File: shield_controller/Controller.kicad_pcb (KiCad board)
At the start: 2 copper layers, 68.6 x 53.3 mm, 16 parts, among them J1 Input Power, J2 Track, J3 DCC, J4 Calc, U1 LM7805_TO220, U2 LMD18200T

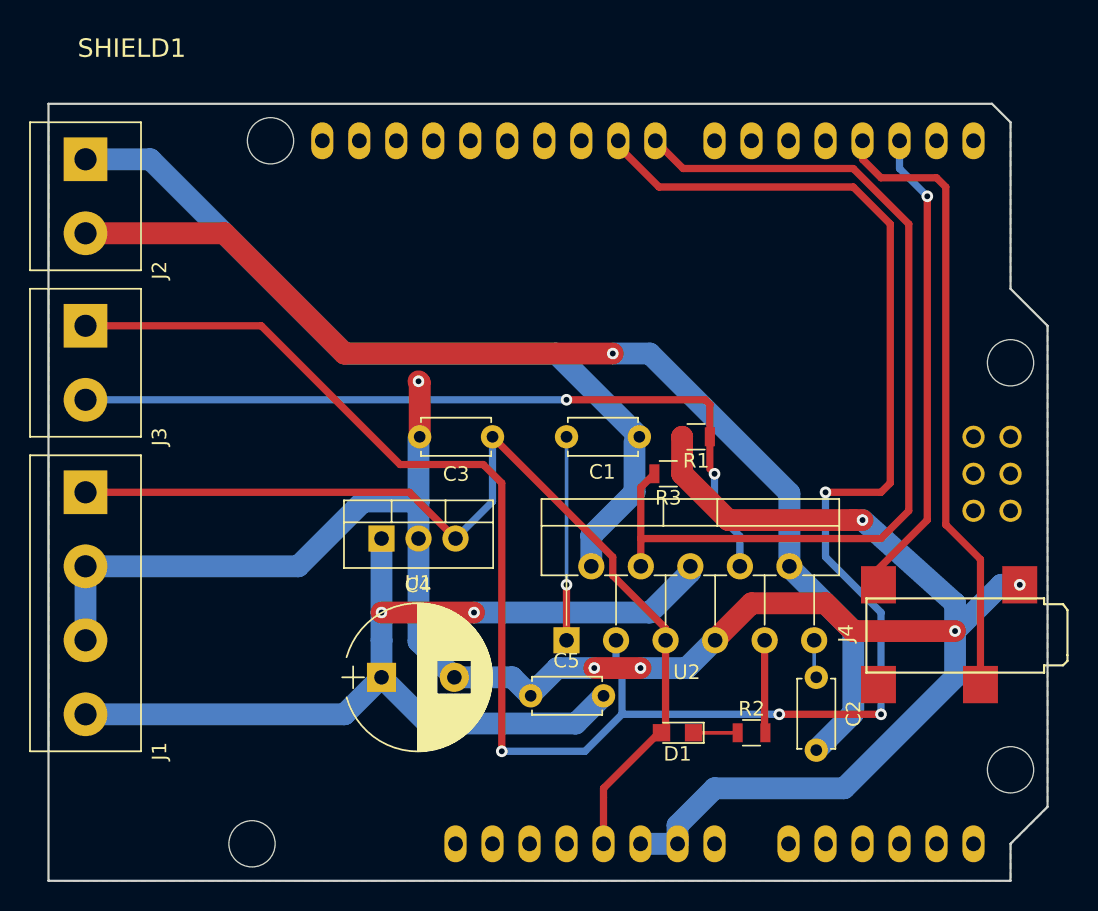
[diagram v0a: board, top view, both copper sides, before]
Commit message: Updating Christopher's shield controller to current fabbed version
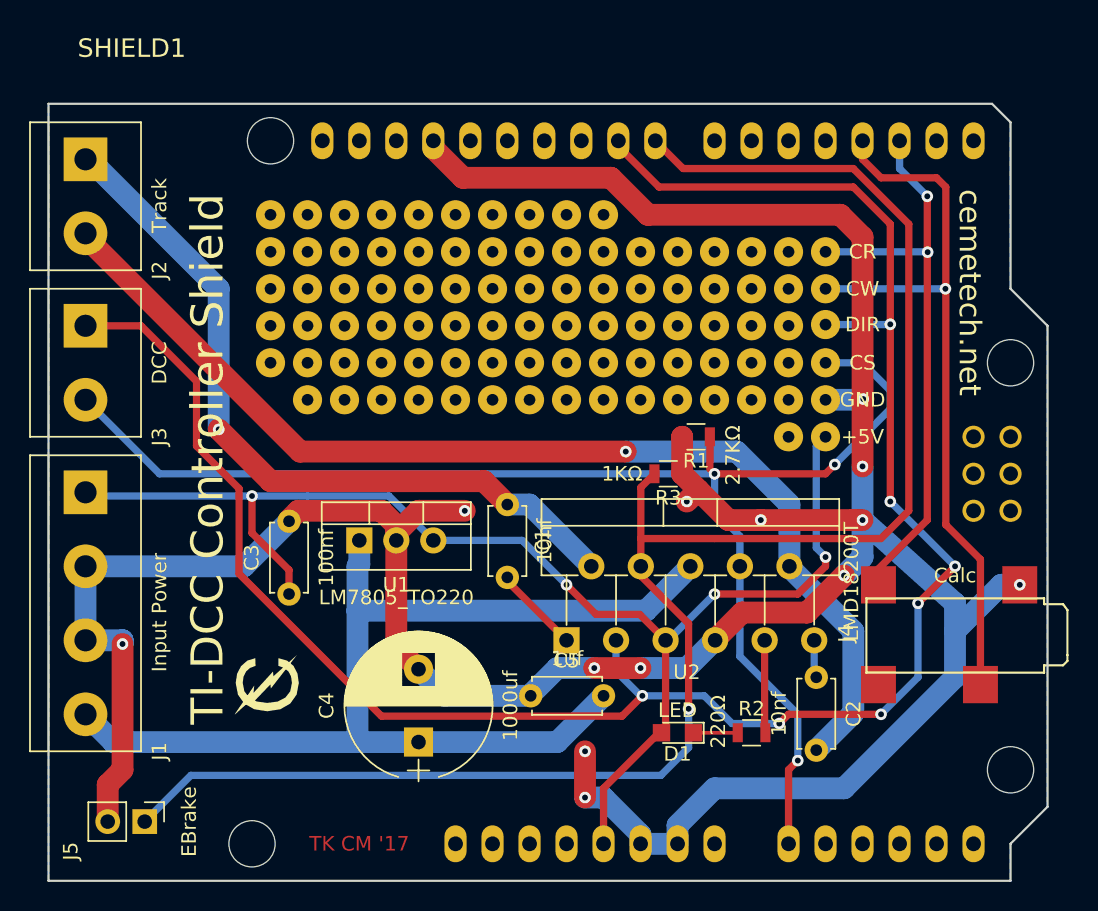
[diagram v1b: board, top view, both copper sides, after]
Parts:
- added ?: , Wire_Pads:SolderWirePad_single_0-8mmDrill, F.Cu at (149.9, 73.7)
- added ?: , Wire_Pads:SolderWirePad_single_0-8mmDrill, F.Cu at (162.6, 63.5)
- added ?: , Wire_Pads:SolderWirePad_single_0-8mmDrill, F.Cu at (165.1, 63.5)
- added ?: , Wire_Pads:SolderWirePad_single_0-8mmDrill, F.Cu at (167.6, 63.5)
- added ?: , Wire_Pads:SolderWirePad_single_0-8mmDrill, F.Cu at (170.2, 63.5)
- added ?: , Wire_Pads:SolderWirePad_single_0-8mmDrill, F.Cu at (172.7, 63.5)
- added ?: , Wire_Pads:SolderWirePad_single_0-8mmDrill, F.Cu at (152.4, 76.2)
- added ?: , Wire_Pads:SolderWirePad_single_0-8mmDrill, F.Cu at (154.9, 76.2)
- added ?: , Wire_Pads:SolderWirePad_single_0-8mmDrill, F.Cu at (157.5, 76.2)
- added ?: , Wire_Pads:SolderWirePad_single_0-8mmDrill, F.Cu at (160.0, 76.2)
- added ?: , Wire_Pads:SolderWirePad_single_0-8mmDrill, F.Cu at (162.6, 76.2)
- added ?: , Wire_Pads:SolderWirePad_single_0-8mmDrill, F.Cu at (149.9, 71.1)
- added ?: , Wire_Pads:SolderWirePad_single_0-8mmDrill, F.Cu at (165.1, 76.2)
- added ?: , Wire_Pads:SolderWirePad_single_0-8mmDrill, F.Cu at (167.6, 76.2)
- added ?: , Wire_Pads:SolderWirePad_single_0-8mmDrill, F.Cu at (170.2, 76.2)
- added ?: , Wire_Pads:SolderWirePad_single_0-8mmDrill, F.Cu at (172.7, 76.2)
- added ?: , Wire_Pads:SolderWirePad_single_0-8mmDrill, F.Cu at (175.3, 76.2)
- added ?: , Wire_Pads:SolderWirePad_single_0-8mmDrill, F.Cu at (177.8, 76.2)
- added ?: , Wire_Pads:SolderWirePad_single_0-8mmDrill, F.Cu at (180.3, 76.2)
- added ?: , Wire_Pads:SolderWirePad_single_0-8mmDrill, F.Cu at (182.9, 76.2)
- added ?: , Wire_Pads:SolderWirePad_single_0-8mmDrill, F.Cu at (185.4, 78.7)
- added ?: , Wire_Pads:SolderWirePad_4xSquare_0-8mmDrill, F.Cu at (184.2, 67.3)
- added ?: , Wire_Pads:SolderWirePad_single_0-8mmDrill, F.Cu at (149.9, 68.6)
- added ?: , Wire_Pads:SolderWirePad_4xSquare_0-8mmDrill, F.Cu at (184.2, 72.4)
- added ?: , Wire_Pads:SolderWirePad_4xSquare_0-8mmDrill, F.Cu at (179.1, 67.3)
- added ?: , Wire_Pads:SolderWirePad_4xSquare_0-8mmDrill, F.Cu at (179.1, 72.4)
- added ?: , Wire_Pads:SolderWirePad_4xSquare_0-8mmDrill, F.Cu at (174.0, 72.4)
- added ?: , Wire_Pads:SolderWirePad_4xSquare_0-8mmDrill, F.Cu at (168.9, 72.4)
- added ?: , Wire_Pads:SolderWirePad_4xSquare_0-8mmDrill, F.Cu at (163.8, 72.4)
- added ?: , Wire_Pads:SolderWirePad_4xSquare_0-8mmDrill, F.Cu at (158.8, 72.4)
- added ?: , Wire_Pads:SolderWirePad_4xSquare_0-8mmDrill, F.Cu at (153.7, 72.4)
- added ?: , Wire_Pads:SolderWirePad_4xSquare_0-8mmDrill, F.Cu at (174.0, 67.3)
- added ?: , Wire_Pads:SolderWirePad_4xSquare_0-8mmDrill, F.Cu at (168.9, 67.3)
- added ?: , Wire_Pads:SolderWirePad_single_0-8mmDrill, F.Cu at (149.9, 66.0)
- added ?: , Wire_Pads:SolderWirePad_4xSquare_0-8mmDrill, F.Cu at (163.8, 67.3)
- added ?: , Wire_Pads:SolderWirePad_4xSquare_0-8mmDrill, F.Cu at (158.8, 67.3)
- added ?: , Wire_Pads:SolderWirePad_4xSquare_0-8mmDrill, F.Cu at (153.7, 67.3)
- added ?: CR, Wire_Pads:SolderWirePad_single_0-8mmDrill, F.Cu at (188.0, 66.0)
- added ?: CW, Wire_Pads:SolderWirePad_single_0-8mmDrill, F.Cu at (188.0, 68.6)
- added ?: DIR, Wire_Pads:SolderWirePad_single_0-8mmDrill, F.Cu at (188.0, 71.0)
- added ?: CS, Wire_Pads:SolderWirePad_single_0-8mmDrill, F.Cu at (188.0, 73.7)
- added ?: +5V, Wire_Pads:SolderWirePad_single_0-8mmDrill, F.Cu at (188.0, 78.7)
- added ?: GND, Wire_Pads:SolderWirePad_single_0-8mmDrill, F.Cu at (188.0, 76.2)
- added ?: , Wire_Pads:SolderWirePad_single_0-8mmDrill, F.Cu at (185.4, 76.2)
- added ?: , Wire_Pads:SolderWirePad_single_0-8mmDrill, F.Cu at (149.9, 63.5)
- added ?: , shield_controller:cememod.mod, F.Cu at (149.6, 95.8)
- added ?: , Wire_Pads:SolderWirePad_single_0-8mmDrill, F.Cu at (152.4, 63.5)
- added ?: , Wire_Pads:SolderWirePad_single_0-8mmDrill, F.Cu at (154.9, 63.5)
- added ?: , Wire_Pads:SolderWirePad_single_0-8mmDrill, F.Cu at (157.5, 63.5)
- added ?: , Wire_Pads:SolderWirePad_single_0-8mmDrill, F.Cu at (160.0, 63.5)
- added J5: EBrake, Pin_Headers:Pin_Header_Straight_1x02_Pitch2.54mm, F.Cu at (141.2, 105.2)
- moved C3 17.7 mm to (151.1, 89.5), turned to 90 degrees
- moved C1 10.5 mm to (166.1, 88.4), turned to 90 degrees
- moved C4 5.12 mm to (160.0, 99.7), turned to 90 degrees
- moved U1 1.53 mm to (156.0, 85.9)
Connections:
- SHIELD1 pad AD0: Net-(SHIELD1-PadAD0) -> /Current_Sense
- SHIELD1 pad GND3: Net-(SHIELD1-PadGND3) -> GND
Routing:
- net GND: track 152.8 -> 226.0 mm, vias 6 -> 13
- net /Brake: track 66.0 -> 119.3 mm, vias 0 -> 1
- net /Current_Sense: track 55.0 -> 96.4 mm, vias 2 -> 3
- net +5V: track 70.3 -> 90.3 mm, vias 0 -> 4
- net /CalcWhite: track 42.9 -> 51.2 mm, vias 0 -> 1
- net Net-(C1-Pad1): track 14.0 -> 6.00 mm, vias 1 -> 0
- net /CalcRed: track 33.1 -> 40.2 mm, vias 1 -> 2
- net +12V: track 71.0 -> 75.7 mm, vias 2 -> 0
- net /Track1: track 56.2 -> 51.9 mm, vias 0 -> 1
- net /Direction: track 146.0 -> 144.2 mm, vias 4 -> 7
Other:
- board text added: "2017-12-22"
- board text added: "TI-DCC Controller Shield"
- board text added: "TI-DCC Controller Shield v0.1a"
- board text added: "TK CM '17"
- board text added: "cemetech.net"
